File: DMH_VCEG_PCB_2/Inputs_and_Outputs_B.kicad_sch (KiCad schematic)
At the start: 44 parts, among them J11 TS_Jack_6.35mm_Sw, J12 TS_Jack_6.35mm_Sw, J13 TS_Jack_6.35mm_Sw, J14 TS_Jack_6.35mm_Sw, J15 TS_Jack_6.35mm_Sw, J16 TS_Jack_6.35mm_Sw, J17 TS_Jack_6.35mm_Sw, J18 TS_Jack_6.35mm_Sw, J19 TS_Jack_6.35mm_Sw, J20 TS_Jack_6.35mm_Sw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

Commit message: PCB 2 routing in progress
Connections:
- net Att CV B: no longer J27.3 (Pin_3)
- net Dec CV B: no longer J27.6 (Pin_6)
- net Rel CV B: no longer J27.10 (Pin_10)
- net Sus CV B: no longer J27.7 (Pin_7)
- no-connect marks 0 -> 4
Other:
- moved on the sheet: J27C, J27F, J27G, J27J
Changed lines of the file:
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@@
 	)
 	(junction
-		(at 144.78 129.54)
-		(diameter 0)
-		(color 0 0 0 0)
-	)
-	(junction
 		(at 176.53 215.9)
 		(diameter 0)
@@
 	)
 	(junction
-		(at 144.78 66.04)
-		(diameter 0)
-		(color 0 0 0 0)
-	)
-	(junction
-		(at 144.78 34.29)
-		(diameter 0)
-		(color 0 0 0 0)
-	)
-	(junction
 		(at 115.57 63.5)
 		(diameter 0)
@@
 	)
 	(junction
-		(at 144.78 97.79)
-		(diameter 0)
-		(color 0 0 0 0)
-	)
-	(junction
 		(at 125.73 175.26)
 		(diameter 0)
@@
 		(color 0 0 0 0)
 	)
+	(no_connect
+		(at 144.78 63.5)
+	)
+	(no_connect
+		(at 144.78 127)
+	)
+	(no_connect
+		(at 144.78 31.75)
+	)
+	(no_connect
+		(at 144.78 95.25)
+	)
 	(wire
 		(pts
@@
 	(wire
 		(pts
-			(xy 144.78 97.79) (xy 158.75 97.79)
+			(xy 138.43 97.79) (xy 158.75 97.79)
 		)
 		(stroke
@@
 	(wire
 		(pts
-			(xy 144.78 66.04) (xy 158.75 66.04)
+			(xy 138.43 66.04) (xy 158.75 66.04)
 		)
 		(stroke
@@
 	(wire
 		(pts
-			(xy 138.43 66.04) (xy 144.78 66.04)
-		)
-		(stroke
-			(width 0)
-			(type default)
-		)
-	)
-	(wire
-		(pts
 			(xy 105.41 231.14) (xy 109.22 231.14)
 		)
@@
 	(wire
 		(pts
-			(xy 138.43 97.79) (xy 144.78 97.79)
-		)
-		(stroke
-			(width 0)
-			(type default)
-		)
-	)
-	(wire
-		(pts
 			(xy 38.1 149.86) (xy 38.1 175.26)
 		)
@@
 	(wire
 		(pts
-			(xy 144.78 129.54) (xy 158.75 129.54)
+			(xy 138.43 129.54) (xy 158.75 129.54)
 		)
 		(stroke
@@
 	(wire
 		(pts
-			(xy 144.78 34.29) (xy 158.75 34.29)
+			(xy 138.43 34.29) (xy 158.75 34.29)
 		)
 		(stroke
@@
 	(wire
 		(pts
-			(xy 138.43 34.29) (xy 144.78 34.29)
-		)
-		(stroke
-			(width 0)
-			(type default)
-		)
-	)
-	(wire
-		(pts
 			(xy 44.45 228.6) (xy 30.48 228.6)
 		)
@@
 	(wire
 		(pts
-			(xy 138.43 129.54) (xy 144.78 129.54)
-		)
-		(stroke
-			(width 0)
-			(type default)
-		)
-	)
-	(wire
-		(pts
 			(xy 132.08 228.6) (xy 142.24 228.6)
 		)
@@
 	(symbol
 		(lib_id "SynthStuff:Conn_01x10_PinHeader")
-		(at 144.78 124.46 270)
+		(at 144.78 121.92 270)
 		(unit 10)
 		(exclude_from_sim no)
@@
 		(fields_autoplaced yes)
 		(property "Reference" "J27"
-			(at 146.05 125.0949 90)
+			(at 146.05 122.5549 90)
 			(effects
 				(font
@@
 		)
 		(property "Value" "Conn_01x10_PinHeader"
-			(at 142.24 124.46 0)
+			(at 142.24 121.92 0)
 			(effects
 				(font
@@
 		)
 		(property "Footprint" "Connector_PinSocket_2.54mm:PinSocket_1x10_P2.54mm_Vertical"
-			(at 144.78 124.46 0)
+			(at 144.78 121.92 0)
 			(effects
 				(font
@@
 		)
 		(property "Datasheet" "~"
-			(at 144.78 124.46 0)
+			(at 144.78 121.92 0)
 			(effects
 				(font
@@
 		)
 		(property "Description" "Generic connector, single row, 01x10"
-			(at 144.78 124.46 0)
+			(at 144.78 121.92 0)
 			(effects
 				(font
@@
 	(symbol
 		(lib_id "SynthStuff:Conn_01x10_PinHeader")
-		(at 144.78 92.71 270)
+		(at 144.78 90.17 270)
 		(unit 7)
 		(exclude_from_sim no)
@@
 		(fields_autoplaced yes)
 		(property "Reference" "J27"
-			(at 146.05 93.3449 90)
+			(at 146.05 90.8049 90)
 			(effects
 				(font
@@
 		)
 		(property "Value" "Conn_01x10_PinHeader"
-			(at 142.24 92.71 0)
+			(at 142.24 90.17 0)
 			(effects
 				(font
@@
 		)
 		(property "Footprint" "Connector_PinSocket_2.54mm:PinSocket_1x10_P2.54mm_Vertical"
-			(at 144.78 92.71 0)
+			(at 144.78 90.17 0)
 			(effects
 				(font
@@
 		)
 		(property "Datasheet" "~"
-			(at 144.78 92.71 0)
+			(at 144.78 90.17 0)
 			(effects
 				(font
@@
 		)
 		(property "Description" "Generic connector, single row, 01x10"
-			(at 144.78 92.71 0)
+			(at 144.78 90.17 0)
 			(effects
 				(font
@@
 	(symbol
 		(lib_id "SynthStuff:Conn_01x10_PinHeader")
-		(at 144.78 29.21 270)
+		(at 144.78 26.67 270)
 		(unit 3)
 		(exclude_from_sim no)
@@
 		(fields_autoplaced yes)
 		(property "Reference" "J27"
-			(at 146.05 29.8449 90)
+			(at 146.05 27.3049 90)
 			(effects
 				(font
@@
 		)
 		(property "Value" "Conn_01x10_PinHeader"
-			(at 142.24 29.21 0)
+			(at 142.24 26.67 0)
 			(effects
 				(font
@@
 		)
 		(property "Footprint" "Connector_PinSocket_2.54mm:PinSocket_1x10_P2.54mm_Vertical"
-			(at 144.78 29.21 0)
+			(at 144.78 26.67 0)
 			(effects
 				(font
@@
 		)
 		(property "Datasheet" "~"
-			(at 144.78 29.21 0)
+			(at 144.78 26.67 0)
 			(effects
 				(font
@@
 		)
 		(property "Description" "Generic connector, single row, 01x10"
-			(at 144.78 29.21 0)
+			(at 144.78 26.67 0)
 			(effects
 				(font
@@
 	(symbol
 		(lib_id "SynthStuff:Conn_01x10_PinHeader")
-		(at 144.78 60.96 270)
+		(at 144.78 58.42 270)
 		(unit 6)
 		(exclude_from_sim no)
@@
 		(fields_autoplaced yes)
 		(property "Reference" "J27"
-			(at 146.05 61.5949 90)
+			(at 146.05 59.0549 90)
 			(effects
 				(font
@@
 		)
 		(property "Value" "Conn_01x10_PinHeader"
-			(at 142.24 60.96 0)
+			(at 142.24 58.42 0)
 			(effects
 				(font
@@
 		)
 		(property "Footprint" "Connector_PinSocket_2.54mm:PinSocket_1x10_P2.54mm_Vertical"
-			(at 144.78 60.96 0)
+			(at 144.78 58.42 0)
 			(effects
 				(font
@@
 		)
 		(property "Datasheet" "~"
-			(at 144.78 60.96 0)
+			(at 144.78 58.42 0)
 			(effects
 				(font
@@
 		)
 		(property "Description" "Generic connector, single row, 01x10"
-			(at 144.78 60.96 0)
+			(at 144.78 58.42 0)
 			(effects
 				(font

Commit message: Restarted component placing on Main
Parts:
- removed unit 10 of J27
- removed unit 7 of J27
- removed unit 3 of J27
- removed unit 6 of J27
- renumbered J27 to J26
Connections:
- net Att CV B: now also U23.14; no longer U23.1
- net Rel CV B: now also U23.8; no longer U23.14
- net SG Out B: now also J26.4 (Pin_4); no longer J26.2 (Pin_2)
- net Sus CV B: now also U23.1; no longer U23.8
- net at R183.2, RV36.1: now also U23.2 (-); no longer U23.9 (-)
- net at J14.T, R184.1, RV39.3: now also J27.8 (Pin_8); no longer J27.9 (Pin_9)
- net at J11.T, R181.1, RV33.3: now also J26.2 (Pin_2); no longer J26.4 (Pin_4)
- net at R185.1, R186.2: now also U18.2 (-); no longer U18.13 (-)
- net at R185.2, R187.2: now also U18.1; no longer U18.14
- net at R181.2, RV32.1: now also U23.13 (-); no longer U23.2 (-)
- net at RV33.2: now also U23.12 (+); no longer U23.3 (+)
- net at R11.1, R18.2: now also U18.3 (+); no longer U18.12 (+)
- net at R184.2, RV38.1: now also U23.9 (-); no longer U23.13 (-)
- net at J13.T, R183.1, RV37.3: now also J27.3 (Pin_3); no longer J27.8 (Pin_8)
- net at RV39.2: now also U23.10 (+); no longer U23.12 (+)
- net at RV37.2: now also U23.3 (+); no longer U23.10 (+)
- no-connect marks 4 -> 0

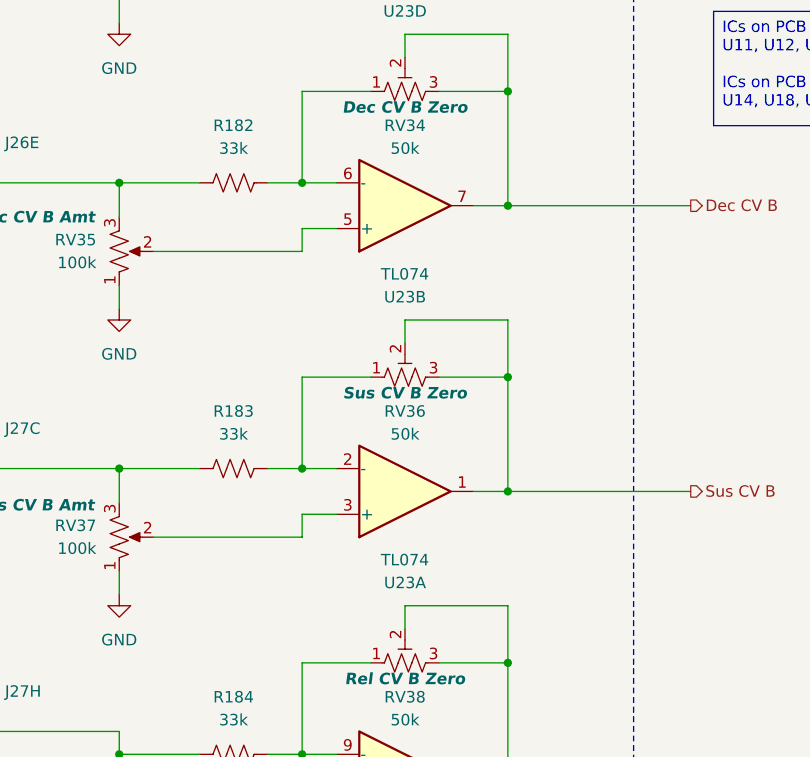
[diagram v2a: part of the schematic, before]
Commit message: PCB 2 placement in progress
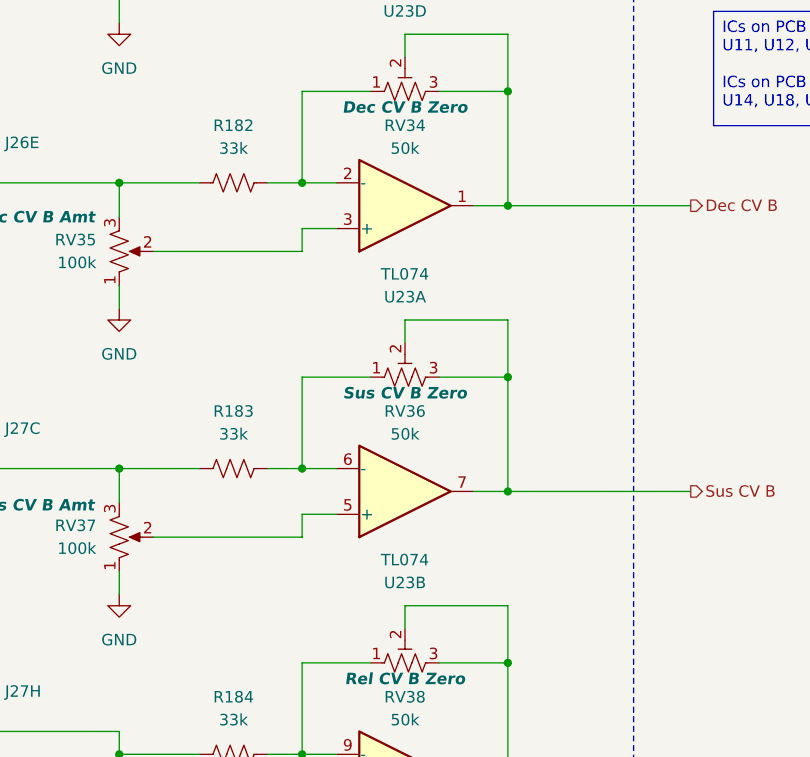
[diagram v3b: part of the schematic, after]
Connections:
- net Dec CV B: now also U23.1; no longer U23.7
- net Sus CV B: now also U23.7; no longer U23.1
- net at R183.2, RV36.1: now also U23.6 (-); no longer U23.2 (-)
- net at R182.2, RV34.1: now also U23.2 (-); no longer U23.6 (-)
- net at RV35.2: now also U23.3 (+); no longer U23.5 (+)
- net at RV37.2: now also U23.5 (+); no longer U23.3 (+)
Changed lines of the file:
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@@
 		(at 127 66.04 0)
 		(mirror x)
-		(unit 2)
+		(unit 1)
 		(exclude_from_sim no)
 		(in_bom yes)
@@
 				(path "/58f4306d-5387-4983-bb08-41a2313fd315/56bd3f35-094b-4adb-8c6d-1e57b38bb61e"
 					(reference "U23")
-					(unit 2)
+					(unit 1)
 				)
 			)
@@
 		(at 127 97.79 0)
 		(mirror x)
-		(unit 1)
+		(unit 2)
 		(exclude_from_sim no)
 		(in_bom yes)
@@
 				(path "/58f4306d-5387-4983-bb08-41a2313fd315/56bd3f35-094b-4adb-8c6d-1e57b38bb61e"
 					(reference "U23")
-					(unit 1)
-				)
-			)
+					(unit 2)
+				)
+			)

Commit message: PCB 2 placement done
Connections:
- net SG Out B: now also J26.5 (Pin_5); no longer J26.4 (Pin_4)
- net at J12.T, R182.1, RV35.3: now also J26.4 (Pin_4); no longer J26.5 (Pin_5)
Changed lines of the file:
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@@
 		(lib_id "SynthStuff:Conn_01x10_PinHeader")
 		(at 142.24 170.18 270)
-		(unit 4)
+		(unit 5)
 		(exclude_from_sim no)
 		(in_bom yes)
@@
 				(path "/58f4306d-5387-4983-bb08-41a2313fd315/56bd3f35-094b-4adb-8c6d-1e57b38bb61e"
 					(reference "J26")
-					(unit 4)
+					(unit 5)
 				)
 			)
@@
 		(lib_id "SynthStuff:Conn_01x10_PinHeader")
 		(at 81.28 58.42 270)
-		(unit 5)
+		(unit 4)
 		(exclude_from_sim no)
 		(in_bom yes)
@@
 				(path "/58f4306d-5387-4983-bb08-41a2313fd315/56bd3f35-094b-4adb-8c6d-1e57b38bb61e"
 					(reference "J26")
-					(unit 5)
-				)
-			)
+					(unit 4)
+				)
+			)

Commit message: Synced PCB 1 o PCB 2
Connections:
- net at R194.1, RV42.1: now also U17.10 (+); no longer U17.5 (+)
- net at R188.1, R191.1, RV40.1: now also U17.14; no longer U17.1
- net at R190.2, RV40.2, RV40.3: now also U17.13 (-); no longer U17.2 (-)
- net at R193.1, RV41.1: now also U17.12 (+); no longer U17.3 (+)
- net at R189.1, R191.2: now also U17.9 (-); no longer U17.6 (-)
- net at R189.2, R192.1: now also U17.8; no longer U17.7
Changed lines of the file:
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@@
 		(lib_id "Amplifier_Operational:TL074")
 		(at 165.1 228.6 180)
-		(unit 1)
+		(unit 4)
 		(exclude_from_sim no)
 		(in_bom yes)
@@
 				(path "/58f4306d-5387-4983-bb08-41a2313fd315/56bd3f35-094b-4adb-8c6d-1e57b38bb61e"
 					(reference "U17")
-					(unit 1)
+					(unit 4)
 				)
 			)
@@
 		(lib_id "Amplifier_Operational:TL074")
 		(at 120.65 231.14 180)
-		(unit 2)
+		(unit 3)
 		(exclude_from_sim no)
 		(in_bom yes)
@@
 				(path "/58f4306d-5387-4983-bb08-41a2313fd315/56bd3f35-094b-4adb-8c6d-1e57b38bb61e"
 					(reference "U17")
-					(unit 2)
-				)
-			)
+					(unit 3)
+				)
+			)

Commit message: Found mistake with SG Out offset resistors
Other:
- note added: "Must be inverted"
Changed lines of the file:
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@@
+		)
+	)
+	(rectangle
+		(start 116.84 187.96)
+		(end 134.62 193.04)
+		(stroke
+			(width 0)
+			(type default)
+		)
+		(fill
+			(type none)
+		)
+	)
+	(text "Must be inverted"
+		(exclude_from_sim no)
+		(at 126.746 186.69 0)
+		(effects
+			(font
+				(size 1.27 1.27)
+			)
 		)
 	)
